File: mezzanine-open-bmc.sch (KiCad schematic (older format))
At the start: 4 parts, among them P1 CONN_02X20, P2 CONN_02X20, SW1 PWR, SW2 RST

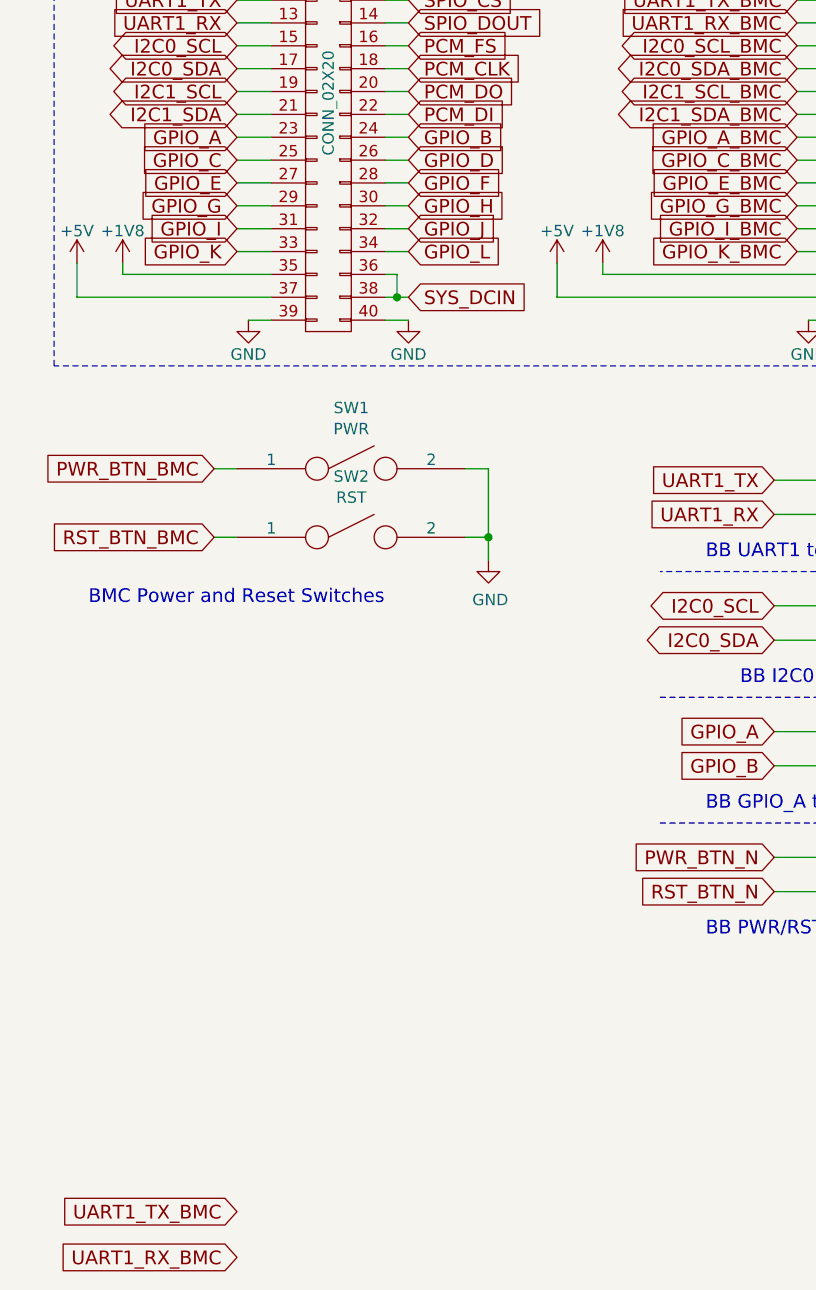
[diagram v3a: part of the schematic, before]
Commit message: Connect BB 1V8 to BMC GPIO_E, Make New Library
The BB 1V8 is wired up to BMC GPIO_E.

Signed-off-by: Sophie Haynes <sophie.haynes@linaro.org>
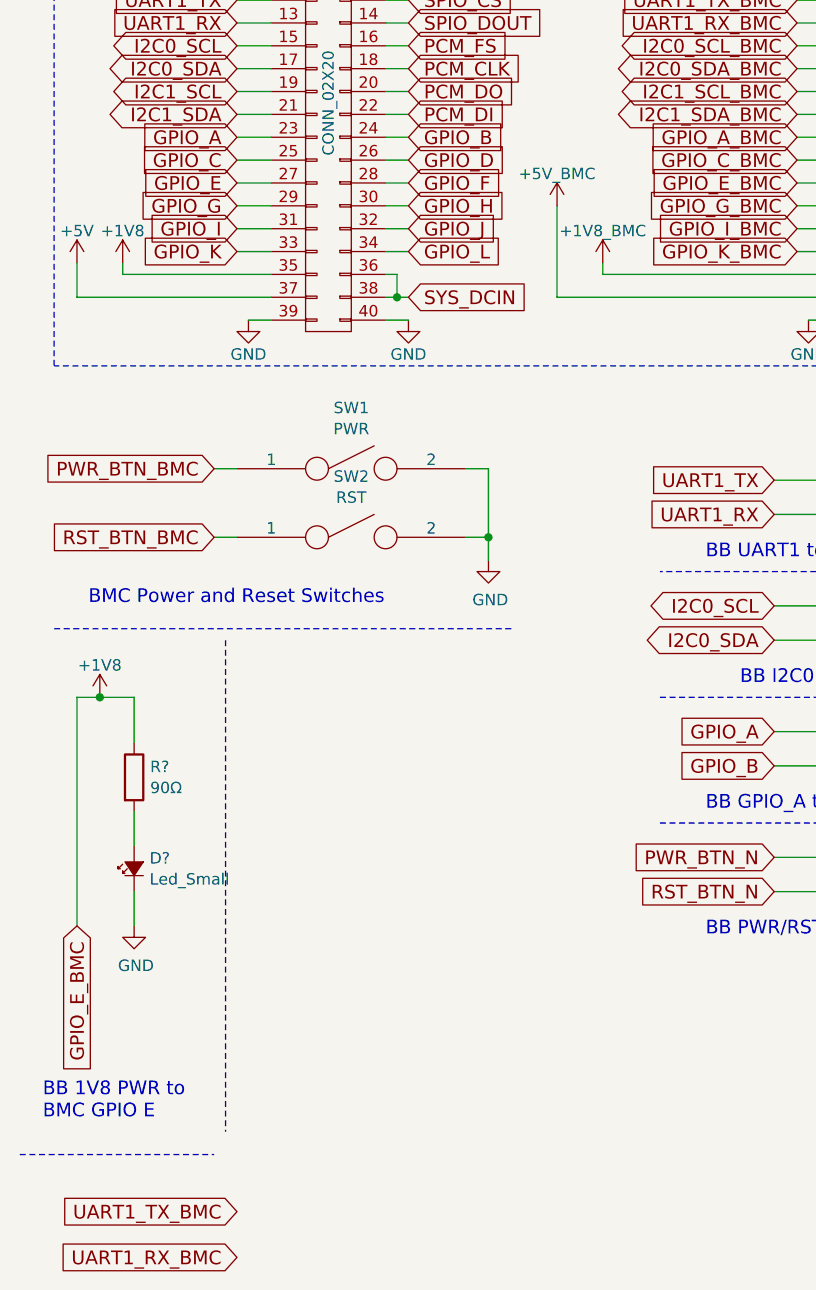
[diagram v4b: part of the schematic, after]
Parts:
- added D?: Led_Small, symbol Led_Small
- added R?: 90Ω, symbol 90Ω
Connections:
- net GPIO_E_BMC is gone; now on net +1V8: P2.27 (P27)
- net +1V8: now also R?.1
- net GND: now also D?.1 (K)
- new net: D?.2 (A), R?.2
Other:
- note added: "BB 1V8 PWR to \nBMC GPIO E"
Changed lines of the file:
@@
 LIBS:valves
 LIBS:96boards
+LIBS:BMC
 LIBS:mezzanine-open-bmc-cache
 EELAYER 25 0
@@
 UART0_RTS_BMC
 $Comp
-L GND #PWR9
+L GND #PWR01
 U 1 1 55D481C7
 P 3950 950
-F 0 "#PWR9" H 3950 700 50  0001 C CNN
+F 0 "#PWR01" H 3950 700 50  0001 C CNN
 F 1 "GND" H 3950 800 50  0000 C CNN
 F 2 "" H 3950 950 60  0000 C CNN
@@
 UART0_TX_BMC
 $Comp
-L GND #PWR10
+L GND #PWR02
 U 1 1 55D481CF
 P 4000 3000
-F 0 "#PWR10" H 4000 2750 50  0001 C CNN
+F 0 "#PWR02" H 4000 2750 50  0001 C CNN
 F 1 "GND" H 4000 2850 50  0000 C CNN
 F 2 "" H 4000 3000 60  0000 C CNN
@@
 $EndComp
 $Comp
-L GND #PWR12
+L GND #PWR03
 U 1 1 55D481D5
 P 4700 3000
-F 0 "#PWR12" H 4700 2750 50  0001 C CNN
+F 0 "#PWR03" H 4700 2750 50  0001 C CNN
 F 1 "GND" H 4700 2850 50  0000 C CNN
 F 2 "" H 4700 3000 60  0000 C CNN
@@
 SYS_DCIN_BMC
 $Comp
-L GND #PWR13
+L GND #PWR04
 U 1 1 55D48218
 P 4750 950
-F 0 "#PWR13" H 4750 700 50  0001 C CNN
+F 0 "#PWR04" H 4750 700 50  0001 C CNN
 F 1 "GND" H 4750 800 50  0000 C CNN
 F 2 "" H 4750 950 60  0000 C CNN
@@
 $EndComp
 $Comp
-L +1V8 #PWR8
+L +1V8_BMC #PWR05
 U 1 1 55D4822C
 P 3100 2750
-F 0 "#PWR8" H 3100 2600 50  0001 C CNN
-F 1 "+1V8" H 3100 2890 50  0000 C CNN
+F 0 "#PWR05" H 3100 2600 50  0001 C CNN
+F 1 "+1V8_BMC" H 3100 2890 50  0000 C CNN
 F 2 "" H 3100 2750 60  0000 C CNN
 F 3 "" H 3100 2750 60  0000 C CNN
@@
 $EndComp
 $Comp
-L +5V #PWR7
+L +5V_BMC #PWR06
 U 1 1 55D48233
-P 2900 2750
-F 0 "#PWR7" H 2900 2600 50  0001 C CNN
-F 1 "+5V" H 2900 2890 50  0000 C CNN
-F 2 "" H 2900 2750 60  0000 C CNN
-F 3 "" H 2900 2750 60  0000 C CNN
-	1    2900 2750
+P 2900 2500
+F 0 "#PWR06" H 2900 2350 50  0001 C CNN
+F 1 "+5V_BMC" H 2900 2640 50  0000 C CNN
+F 2 "" H 2900 2500 60  0000 C CNN
+F 3 "" H 2900 2500 60  0000 C CNN
+	1    2900 2500
 	1    0    0    -1
 $EndComp
@@
 	4100 1500 3950 1500
 $Comp
-L GND #PWR3
+L GND #PWR07
 U 1 1 55BEAA68
 P 1500 950
-F 0 "#PWR3" H 1500 700 50  0001 C CNN
+F 0 "#PWR07" H 1500 700 50  0001 C CNN
 F 1 "GND" H 1500 800 50  0000 C CNN
 F 2 "" H 1500 950 60  0000 C CNN
@@
 $EndComp
 $Comp
-L GND #PWR4
+L GND #PWR08
 U 1 1 55BEA10A
 P 1550 3000
-F 0 "#PWR4" H 1550 2750 50  0001 C CNN
+F 0 "#PWR08" H 1550 2750 50  0001 C CNN
 F 1 "GND" H 1550 2850 50  0000 C CNN
 F 2 "" H 1550 3000 60  0000 C CNN
@@
 $EndComp
 $Comp
-L GND #PWR5
+L GND #PWR09
 U 1 1 55BEA0BC
 P 2250 3000
-F 0 "#PWR5" H 2250 2750 50  0001 C CNN
+F 0 "#PWR09" H 2250 2750 50  0001 C CNN
 F 1 "GND" H 2250 2850 50  0000 C CNN
 F 2 "" H 2250 3000 60  0000 C CNN
@@
 SYS_DCIN
 $Comp
-L GND #PWR6
+L GND #PWR010
 U 1 1 55D43BD4
 P 2300 950
-F 0 "#PWR6" H 2300 700 50  0001 C CNN
+F 0 "#PWR010" H 2300 700 50  0001 C CNN
 F 1 "GND" H 2300 800 50  0000 C CNN
 F 2 "" H 2300 950 60  0000 C CNN
@@
 $EndComp
 $Comp
-L +1V8 #PWR2
+L +1V8 #PWR011
 U 1 1 55D43CFB
 P 1000 2750
-F 0 "#PWR2" H 1000 2600 50  0001 C CNN
+F 0 "#PWR011" H 1000 2600 50  0001 C CNN
 F 1 "+1V8" H 1000 2890 50  0000 C CNN
 F 2 "" H 1000 2750 60  0000 C CNN
@@
 $EndComp
 $Comp
-L +5V #PWR1
+L +5V #PWR012
 U 1 1 55D440FD
 P 800 2750
-F 0 "#PWR1" H 800 2600 50  0001 C CNN
+F 0 "#PWR012" H 800 2600 50  0001 C CNN
 F 1 "+5V" H 800 2890 50  0000 C CNN
 F 2 "" H 800 2750 60  0000 C CNN
@@
 	1400 3950 1500 3950
 $Comp
-L GND #PWR11
+L GND #PWR013
 U 1 1 56D59F1C
 P 2600 4050
-F 0 "#PWR11" H 2600 3800 50  0001 C CNN
+F 0 "#PWR013" H 2600 3800 50  0001 C CNN
 F 1 "GND" H 2608 3876 50  0000 C CNN
 F 2 "" H 2600 4050 50  0000 C CNN
@@
 Wire Wire Line
 	4100 2900 2900 2900
-Wire Wire Line
-	2900 2900 2900 2750
 Text GLabel 1500 6900 0    60   Input ~ 0
 UART1_TX_BMC
@@
 Text Notes 3550 5700 0    60   ~ 0
 BB PWR/RST to BMC GPIO
+Wire Wire Line
+	2900 2900 2900 2500
+$Comp
+L +1V8 #PWR014
+U 1 1 56D5BCFC
+P 900 4650
+F 0 "#PWR014" H 900 4500 50  0001 C CNN
+F 1 "+1V8" H 900 4790 50  0000 C CNN
+F 2 "" H 900 4650 60  0000 C CNN
+F 3 "" H 900 4650 60  0000 C CNN
+	1    900  4650
+	1    0    0    -1
+$EndComp
+Text GLabel 800  5650 3    60   Input ~ 0
+GPIO_E_BMC
+$Comp
+L Led_Small D?
+U 1 1 56D5C019
+P 1050 5400
+F 0 "D?" V 1096 5332 50  0000 R CNN
+F 1 "Led_Small" V 1004 5332 50  0000 R CNN
+F 2 "" V 1050 5400 50  0000 C CNN
+F 3 "" V 1050 5400 50  0000 C CNN
+	1    1050 5400
+	0    -1   -1   0
+$EndComp
+$Comp
+L GND #PWR?
+U 1 1 56D5C06E
+P 1050 5650
+F 0 "#PWR?" H 1050 5400 50  0001 C CNN
+F 1 "GND" H 1058 5476 50  0000 C CNN
+F 2 "" H 1050 5650 50  0000 C CNN
+F 3 "" H 1050 5650 50  0000 C CNN
+	1    1050 5650
+	1    0    0    -1
+$EndComp
+Wire Wire Line
+	800  5650 800  4650
+Wire Wire Line
+	800  4650 1050 4650
+Wire Wire Line
+	1050 4650 1050 4850
+Connection ~ 900  4650
+Wire Wire Line
+	1050 5150 1050 5300
+Wire Wire Line
+	1050 5500 1050 5650
+$Comp
+L 90Ω R?
+U 1 1 56D5C4E6
+P 1050 5000
+F 0 "R?" H 1120 5046 50  0000 L CNN
+F 1 "90Ω" H 1120 4954 50  0000 L CNN
+F 2 "" V 980 5000 50  0000 C CNN
+F 3 "" H 1050 5000 50  0000 C CNN
+	1    1050 5000
+	1    0    0    -1
+$EndComp
+Wire Notes Line
+	700  4350 2700 4350
+Text Notes 650  6500 0    60   ~ 0
+BB 1V8 PWR to \nBMC GPIO E
+Wire Notes Line
+	550  6650 1400 6650
+Wire Notes Line
+	1450 4400 1450 6550
 $EndSCHEMATC

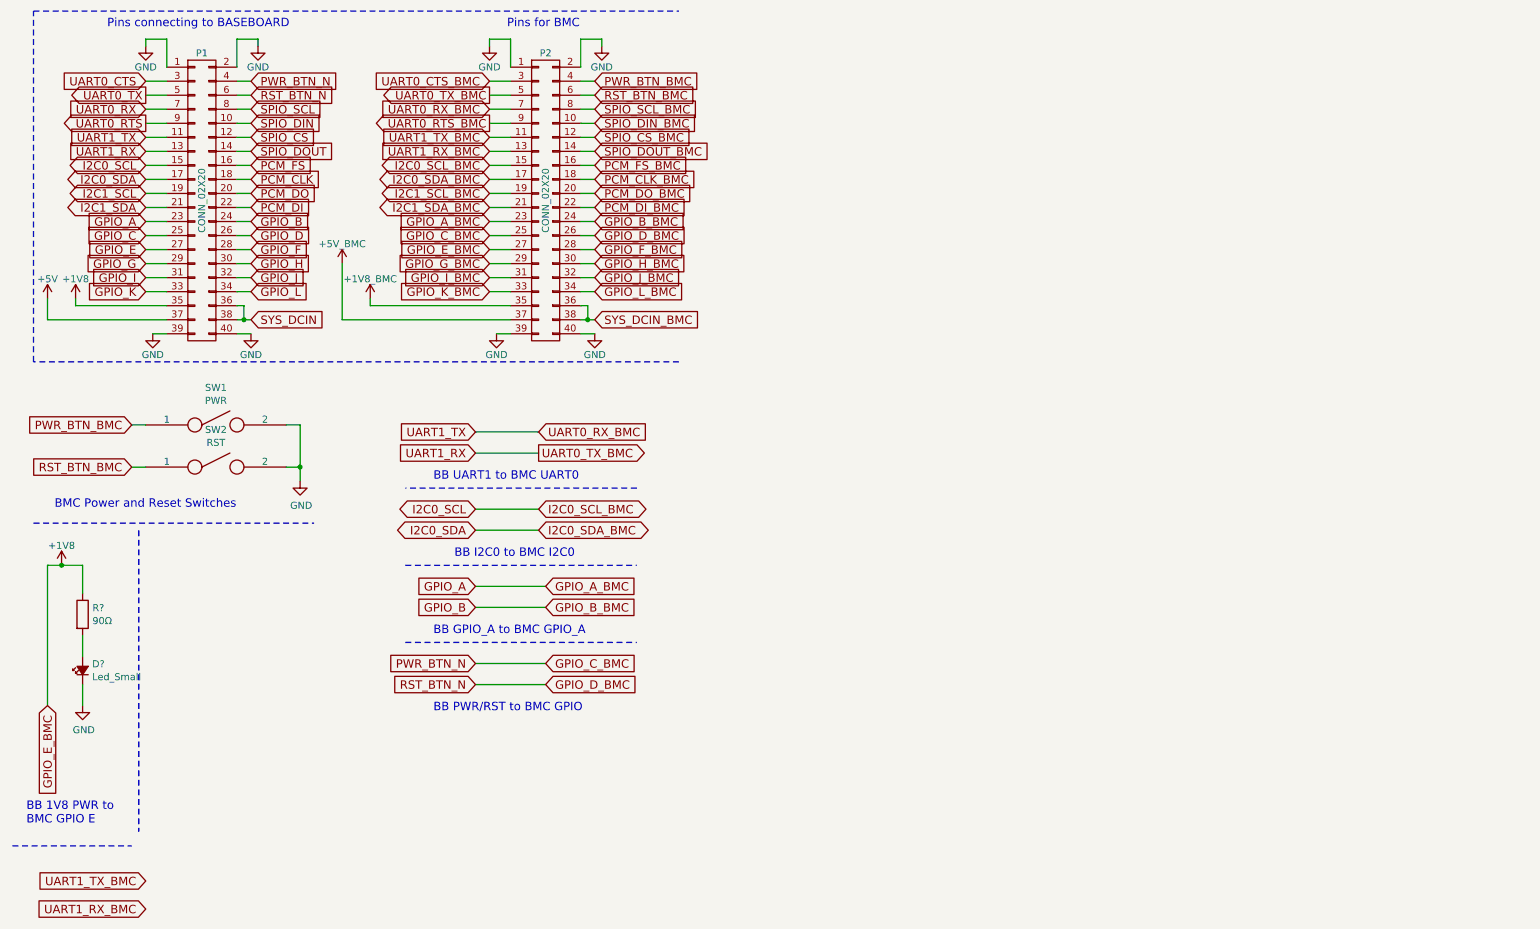
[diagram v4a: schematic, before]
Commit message: Connect FTDI to BMC UART1
A microUSB is now connected to UART1.

Signed-off-by: Sophie Haynes <sophie.haynes@linaro.org>
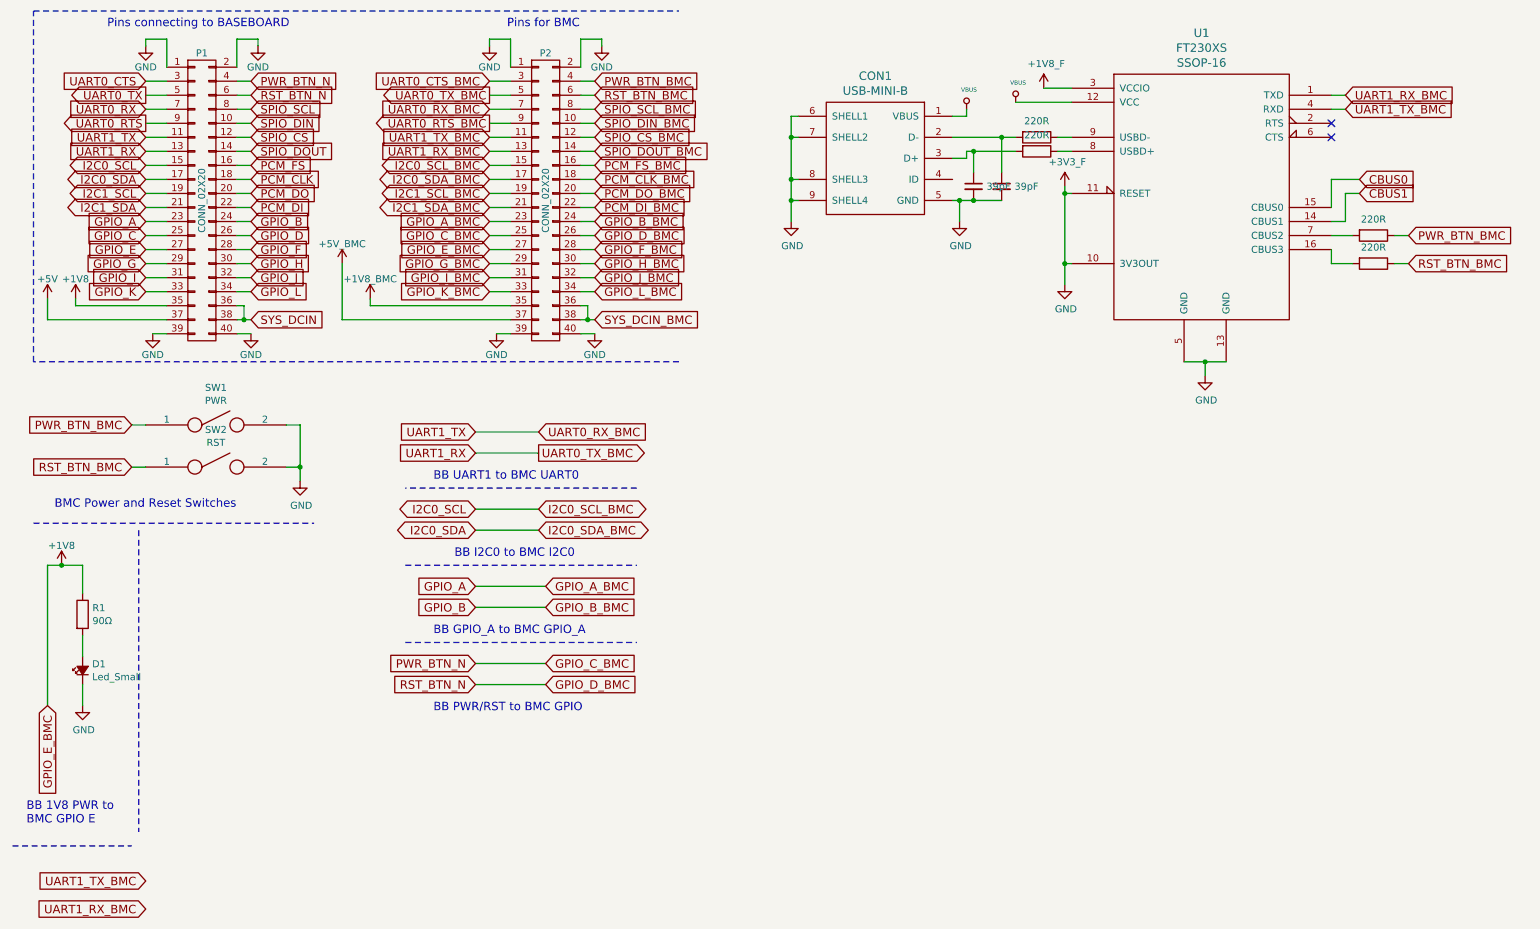
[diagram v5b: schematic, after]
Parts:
- added C? (x2): 39pF, symbol 39pF
- added CON1: USB-MINI-B, symbol USB-MINI-B
- added R2, R3, R? (x2): 220R, symbol 220R
- added U1: FT230XS, SSOP-16, symbol FT230XS
- gave numbers to parts that had none: 2
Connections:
- net +1V8: now also U1.3 (VCCIO)
- net PWR_BTN_BMC: now also R2.1
- net RST_BTN_BMC: now also R3.1
- net UART1_RX_BMC: now also U1.1 (TXD)
- net UART1_TX_BMC: now also U1.4 (RXD)
- net GND renamed +3V3
- net +3V3: now also C?.2, C?.2, CON1.5 (GND), CON1.6 (SHELL1), CON1.7 (SHELL2), CON1.8 (SHELL3), CON1.9 (SHELL4), U1.10 (3V3OUT), U1.11 (RESET), U1.13 (GND), U1.5 (GND)
- new net: R3.2, U1.16 (CBUS3)
- new net: R2.2, U1.7 (CBUS2)
- new net: R?.1, U1.8 (USBD+)
- new net: R?.1, U1.9 (USBD-)
- new net: C?.1, CON1.2 (D-), R?.2
- new net: C?.1, CON1.3 (D+), R?.2
- new net CBUS0: U1.15 (CBUS0)
- new net CBUS1: U1.14 (CBUS1)
- new net VBUS: CON1.1 (VBUS), U1.12 (VCC)
- no-connect marks 0 -> 2
